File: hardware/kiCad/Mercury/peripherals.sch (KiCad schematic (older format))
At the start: 19 parts

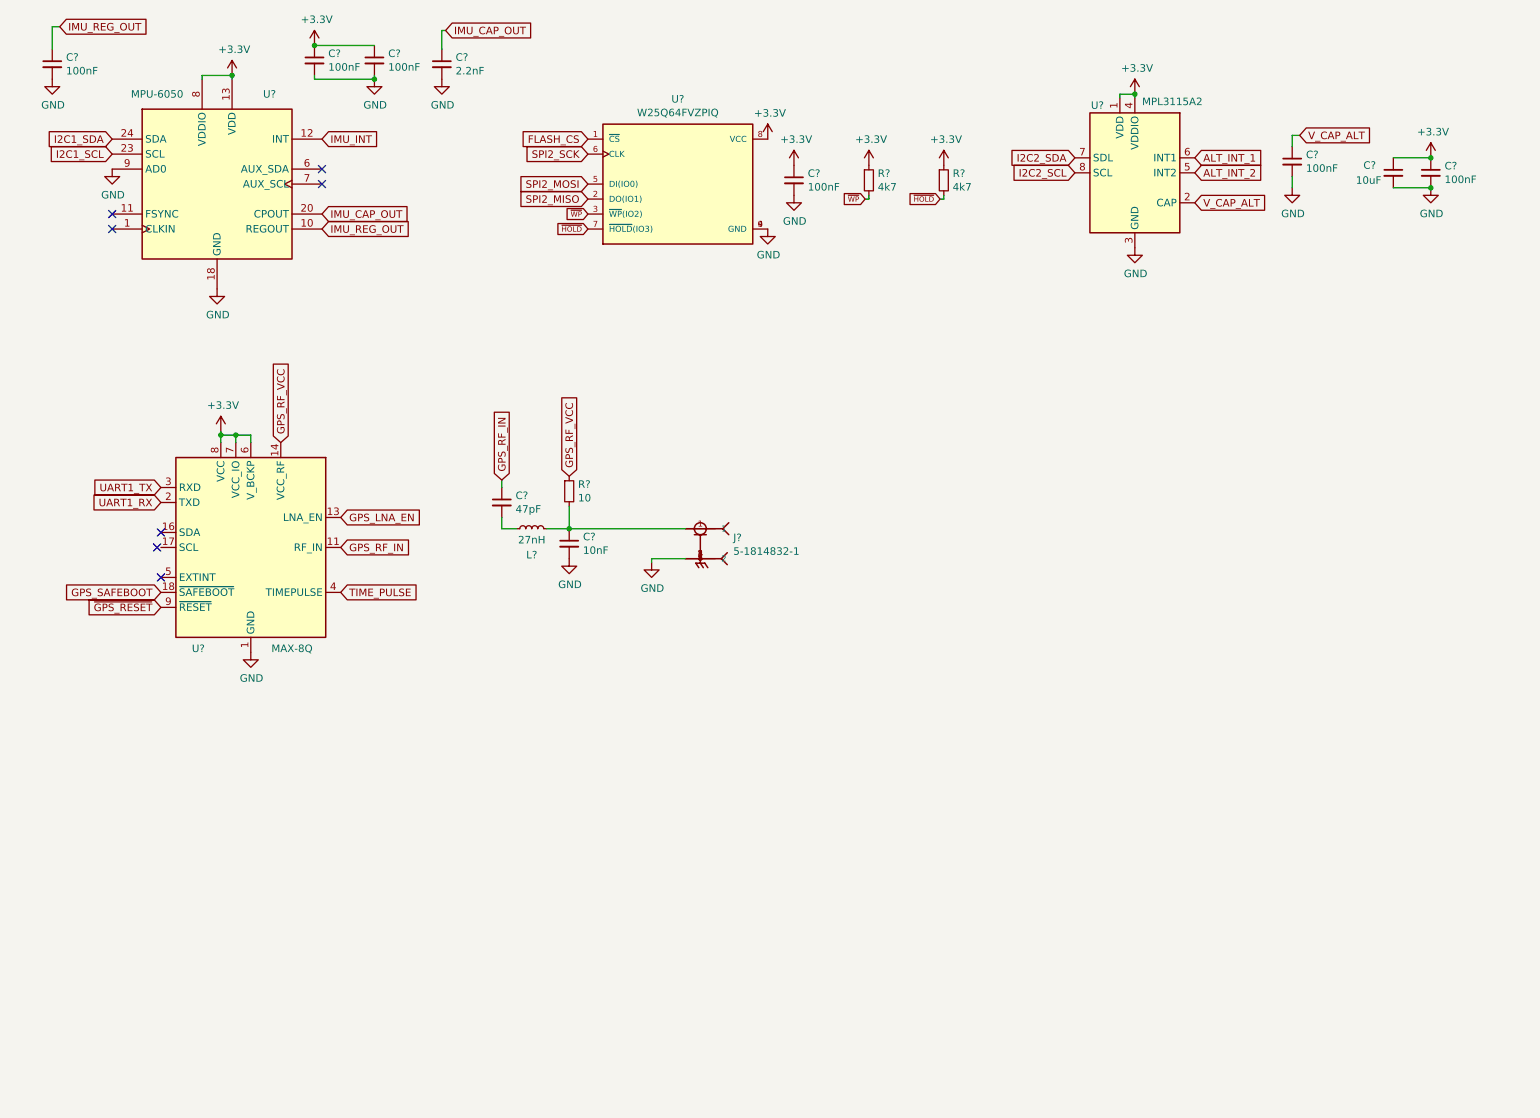
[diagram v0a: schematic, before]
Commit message: Schematic (Minus Connectors) Complete
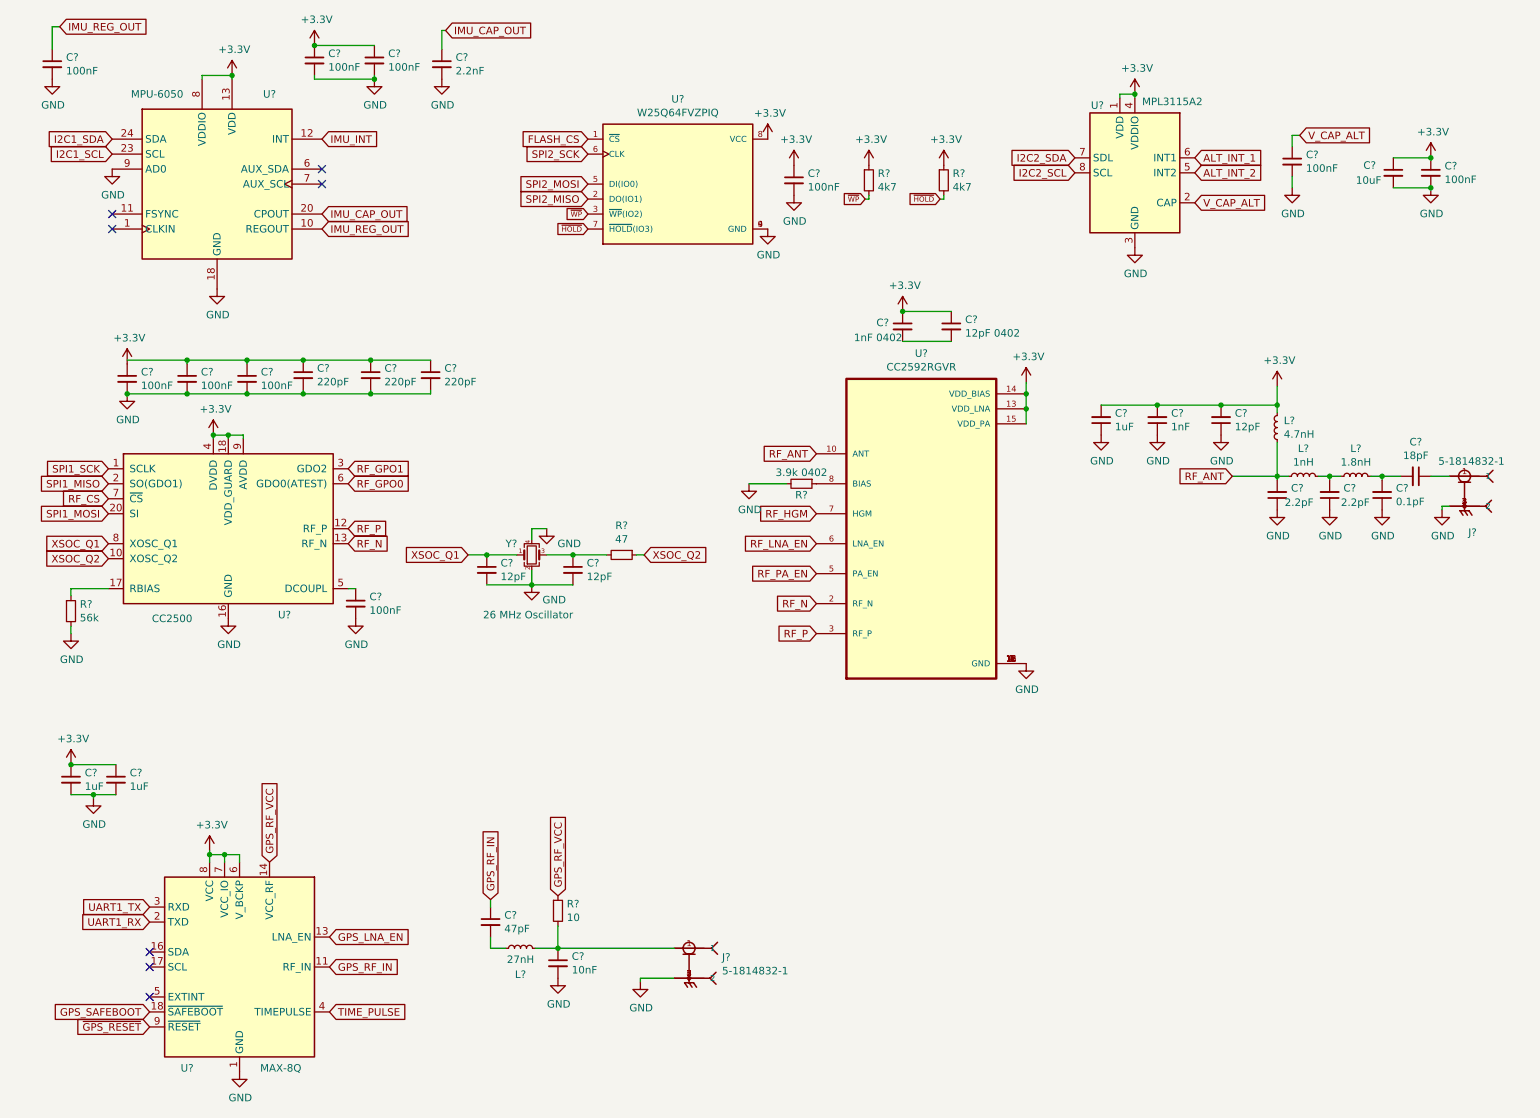
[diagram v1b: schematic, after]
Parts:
- added C?: 1nF 0402, symbol Device:C_Small
- added C?: 12pF 0402, symbol Device:C_Small
- added C?: 18pF, symbol Device:C_Small
- added C?: 0.1pF, symbol Device:C_Small
- added C? (x2): 2.2pF, symbol Device:C_Small
- added C? (x3): 12pF, symbol Device:C_Small
- added C?: 1nF, symbol Device:C_Small
- added C? (x3): 1uF, symbol Device:C_Small
- added C? (x4): 100nF, symbol Device:C_Small
- added C? (x3): 220pF, symbol Device:C_Small
- added J?: 5-1814832-1, TE_5-1814832-1, symbol SMA_ANT:5-1814832-1
- added L?: 1.8nH, symbol Device:L_Small
- added L?: 1nH, symbol Device:L_Small
- added L?: 4.7nH, symbol Device:L_Small
- added R?: 3.9k 0402, symbol Device:R_Small
- added R?: 56k, symbol Device:R_Small
- added R?: 47, symbol Device:R_Small
- added U?: CC2500, Package_DFN_QFN:Texas_S-PVQFN-N20_EP2.4x2.4mm, symbol RF:CC2500
- added U?: CC2592RGVR, QFN65P400X400X100-17N, symbol CC2592:CC2592RGVR
- added Y?: 26 MHz Oscillator, symbol Device:Crystal_GND24_Small
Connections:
- net +3V3: now also C?.1, C?.1, C?.1, C?.1, C?.1, C?.2, C?.2, C?.2, L?.2, U?.11 (AVDD), U?.13 (VDD_LNA), U?.14 (AVDD), U?.14 (VDD_BIAS), U?.15 (AVDD), U?.15 (VDD_PA), U?.18 (VDD_GUARD), U?.4 (DVDD), U?.9 (AVDD)
- net GND: now also C?.1, C?.1, C?.1, C?.1, C?.1, C?.1, C?.2, C?.2, C?.2, C?.2, C?.2, C?.2, C?.2, C?.2, C?.2, C?.2, C?.2, J?.2, J?.3 (2), J?.4 (2), J?.5 (2), R?.2, R?.2, U?.1 (GND), U?.11 (GND), U?.12 (GND), U?.16 (GND), U?.16 (GND), U?.19 (GND), U?.21 (GND), U?.4 (GND), U?.9 (GND), Y?.2, Y?.4
- new net: R?.1, U?.17 (RBIAS)
- new net: C?.1, U?.5 (DCOUPL)
- new net: R?.1, U?.8 (BIAS)
- new net: C?.2, C?.2
- new net: C?.1, J?.1
- new net: C?.2, C?.2, L?.2
- new net: C?.2, L?.1, L?.2
- new net: C?.1, C?.1, C?.1, C?.1, C?.1
- new net: C?.1, R?.2, Y?.3
- new net RF_ANT: C?.2, L?.1, L?.1, U?.10 (ANT)
- new net RF_CS: U?.7 (~CS~)
- new net RF_GPO0: U?.6 (GDO0(ATEST))
- new net RF_GPO1: U?.3 (GDO2)
- new net RF_HGM: U?.7 (HGM)
- new net RF_LNA_EN: U?.6 (LNA_EN)
- new net RF_N: U?.13 (RF_N), U?.2 (RF_N)
- new net RF_P: U?.12 (RF_P), U?.3 (RF_P)
- new net RF_PA_EN: U?.5 (PA_EN)
- new net SPI1_MISO: U?.2 (SO(GDO1))
- new net SPI1_MOSI: U?.20 (SI)
- new net SPI1_SCK: U?.1 (SCLK)
- new net XSOC_Q1: C?.1, U?.8 (XOSC_Q1), Y?.1
- new net XSOC_Q2: R?.1, U?.10 (XOSC_Q2)
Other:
- moved on the sheet: C?, J?, L?, R?, U?

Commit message: Footprints Assigned, Schematic Finalized
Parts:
- removed U?: W25Q64FVZPIQ, SON127P600X500X80-9N, symbol W25Q64FVZPIQ:W25Q64FVZPIQ
- added U5: W25N01GVZEIG_TR, flash:SON127P800X600X80-9N, symbol W25N01GVZEIG:W25N01GVZEIG_TR
- C19, C20, C21, C22, C23, C24, C26: renamed from C?; footprint (none) -> Capacitor_SMD:C_0603_1608Metric
- C25: renamed from C?; footprint (none) -> Capacitor_SMD:C_0805_2012Metric
- C27, C28, C29, C30, C31, C32, C33, C34, C35, C36, C37, C38, C39, C40, C41, C42, C43, C44, C45, C46, C47, C48: renamed from C?; footprint (none) -> Capacitor_SMD:C_0402_1005Metric
- J13, J14: renamed from J?; footprint TE_5-1814832-1 -> SMA_ANT:TE_5-1814832-1
- L2, L3, L4, L5: renamed from L?; footprint (none) -> Inductor_SMD:L_0402_1005Metric
- R32, R33, R34, R35, R36, R37: renamed from R?; footprint (none) -> Resistor_SMD:R_0402_1005Metric
- U8: renamed from U?; footprint QFN65P400X400X100-17N -> CC2592:QFN65P400X400X100-17N
- Y2: renamed from Y?; footprint (none) -> Crystal:Crystal_SMD_3225-4Pin_3.2x2.5mm
- gave numbers to parts that had none: 4
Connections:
- net +3V3: now also U5.8 (VCC)
- net FLASH_CS: now also U5.1 (/CS)
- net GND: now also U5.4 (GND)
- net SPI2_MISO: now also U5.2 (DO(IO1))
- net SPI2_MOSI: now also U5.5 (DI(IO0))
- net SPI2_SCK: now also U5.6 (CLK)
- net ~HOLD: now also U5.7 (/HOLD(IO3))
- net ~WP: now also U5.3 (/WP(IO2))
- net GPS_SAFEBOOT renamed ~GPS_SAFEBOOT
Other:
- moved on the sheet: C23, R32, R33, R37

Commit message: Layout Begins
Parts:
- C19, C20, C21, C23, C24: footprint Capacitor_SMD:C_0603_1608Metric -> Capacitor_SMD:C_0402_1005Metric
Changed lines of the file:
@@
 F 0 "C19" H 792 871 50  0000 L CNN
 F 1 "100nF" H 792 780 50  0000 L CNN
-F 2 "Capacitor_SMD:C_0603_1608Metric" H 700 825 50  0001 C CNN
+F 2 "Capacitor_SMD:C_0402_1005Metric" H 700 825 50  0001 C CNN
 F 3 "~" H 700 825 50  0001 C CNN
 	1    700  825
@@
 F 0 "C21" H 2942 846 50  0000 L CNN
 F 1 "100nF" H 2942 755 50  0000 L CNN
-F 2 "Capacitor_SMD:C_0603_1608Metric" H 2850 800 50  0001 C CNN
+F 2 "Capacitor_SMD:C_0402_1005Metric" H 2850 800 50  0001 C CNN
 F 3 "~" H 2850 800 50  0001 C CNN
 	1    2850 800
@@
 F 0 "C20" H 2542 846 50  0000 L CNN
 F 1 "100nF" H 2542 755 50  0000 L CNN
-F 2 "Capacitor_SMD:C_0603_1608Metric" H 2450 800 50  0001 C CNN
+F 2 "Capacitor_SMD:C_0402_1005Metric" H 2450 800 50  0001 C CNN
 F 3 "~" H 2450 800 50  0001 C CNN
 	1    2450 800
@@
 F 0 "C24" H 9067 1521 50  0000 L CNN
 F 1 "100nF" H 9067 1430 50  0000 L CNN
-F 2 "Capacitor_SMD:C_0603_1608Metric" H 8975 1475 50  0001 C CNN
+F 2 "Capacitor_SMD:C_0402_1005Metric" H 8975 1475 50  0001 C CNN
 F 3 "~" H 8975 1475 50  0001 C CNN
 	1    8975 1475
@@
 F 0 "C23" H 5942 1621 50  0000 L CNN
 F 1 "100nF" H 5942 1530 50  0000 L CNN
-F 2 "Capacitor_SMD:C_0603_1608Metric" H 5850 1575 50  0001 C CNN
+F 2 "Capacitor_SMD:C_0402_1005Metric" H 5850 1575 50  0001 C CNN
 F 3 "~" H 5850 1575 50  0001 C CNN
 	1    5850 1575
